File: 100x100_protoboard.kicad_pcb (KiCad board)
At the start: 2 copper layers, 97.8 x 96.5 mm, 422 parts, among them CON1 BARREL_JACK, CON2 USB_FEMALE_WITH_ID, CON3 USB_FEMALE_WITH_ID, J1 INTERCONNECT_1X03, J10 INTERCONNECT_1X03, J11 INTERCONNECT_1X03, J12 INTERCONNECT_1X03, J13 INTERCONNECT_1X03, J14 INTERCONNECT_1X03, J15 INTERCONNECT_1X03, J16 INTERCONNECT_1X03, J17 INTERCONNECT_1X03, J18 INTERCONNECT_1X03, J19 INTERCONNECT_1X03, J2 INTERCONNECT_1X03, J20 INTERCONNECT_1X03, J21 INTERCONNECT_1X03, J22 INTERCONNECT_1X03, J23 INTERCONNECT_1X03, J24 INTERCONNECT_1X03, J25 INTERCONNECT_1X03, J26 INTERCONNECT_1X03, J27 INTERCONNECT_1X03, J28 INTERCONNECT_1X03, J29 INTERCONNECT_1X03, J3 INTERCONNECT_1X03, J30 INTERCONNECT_1X03, J31 INTERCONNECT_1X03, J32 INTERCONNECT_1X03, J33 INTERCONNECT_1X03, J34 INTERCONNECT_1X03, J35 INTERCONNECT_1X03, J36 INTERCONNECT_1X03, J37 INTERCONNECT_1X03, J38 INTERCONNECT_1X03, J39 INTERCONNECT_1X03, J4 INTERCONNECT_1X03, J40 INTERCONNECT_1X03, J41 INTERCONNECT_1X03, J42 INTERCONNECT_1X03, J43 INTERCONNECT_1X03, J44 INTERCONNECT_1X03, J45 INTERCONNECT_1X03, J46 INTERCONNECT_1X03, J47 INTERCONNECT_1X03, J48 INTERCONNECT_1X03, J49 INTERCONNECT_1X03, J5 INTERCONNECT_1X03, J50 INTERCONNECT_1X03, J51 INTERCONNECT_1X03, J52 INTERCONNECT_1X03, J53 INTERCONNECT_1X03, J54 INTERCONNECT_1X03, J55 INTERCONNECT_1X03, J56 INTERCONNECT_1X03, J57 INTERCONNECT_1X03, J58 INTERCONNECT_1X03, J59 INTERCONNECT_1X03, J6 INTERCONNECT_1X03, J60 INTERCONNECT_1X03, J61 INTERCONNECT_1X03, J62 INTERCONNECT_1X03, J63 INTERCONNECT_1X03, J64 INTERCONNECT_1X03, J65 INTERCONNECT_1X02, J7 INTERCONNECT_1X03, J8 INTERCONNECT_1X03, J9 INTERCONNECT_1X03, P1 CONN_5, P1 CONN_6X2, P2 CONN_6X2, U1 LM7805CT

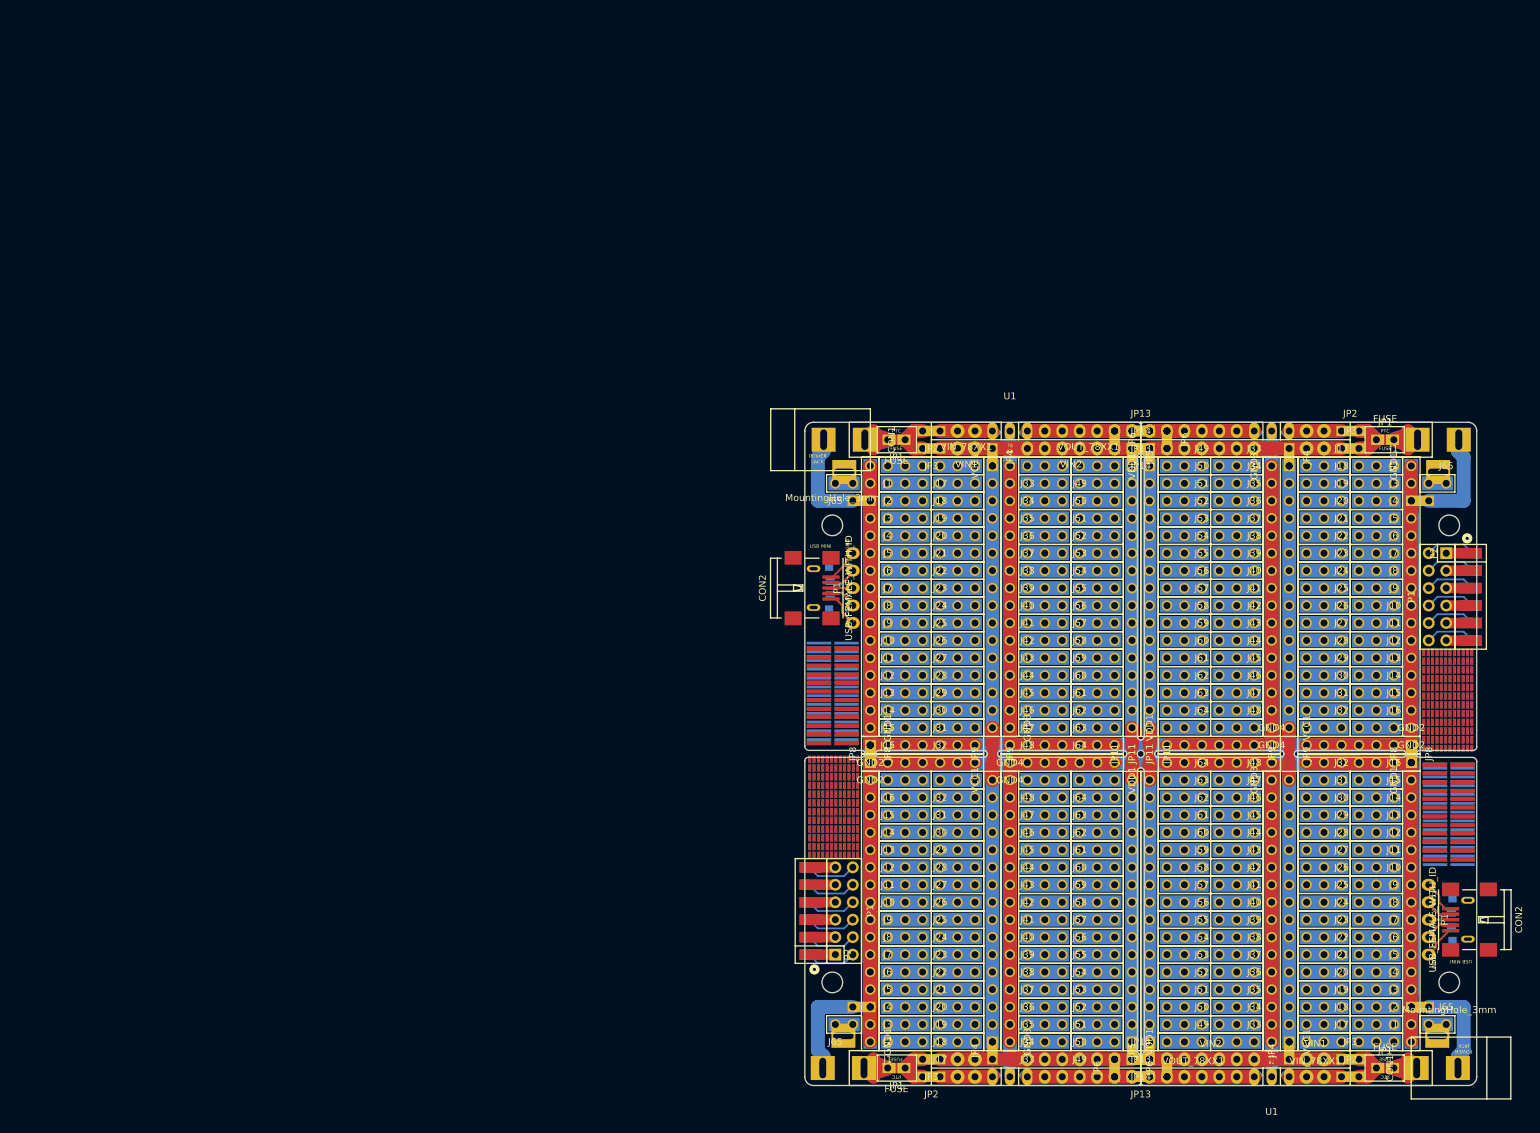
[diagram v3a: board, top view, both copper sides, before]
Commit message: increased .1" edge connector from 2*6 to 2*8 to account for the A-100 system bus used in modular synthesizers
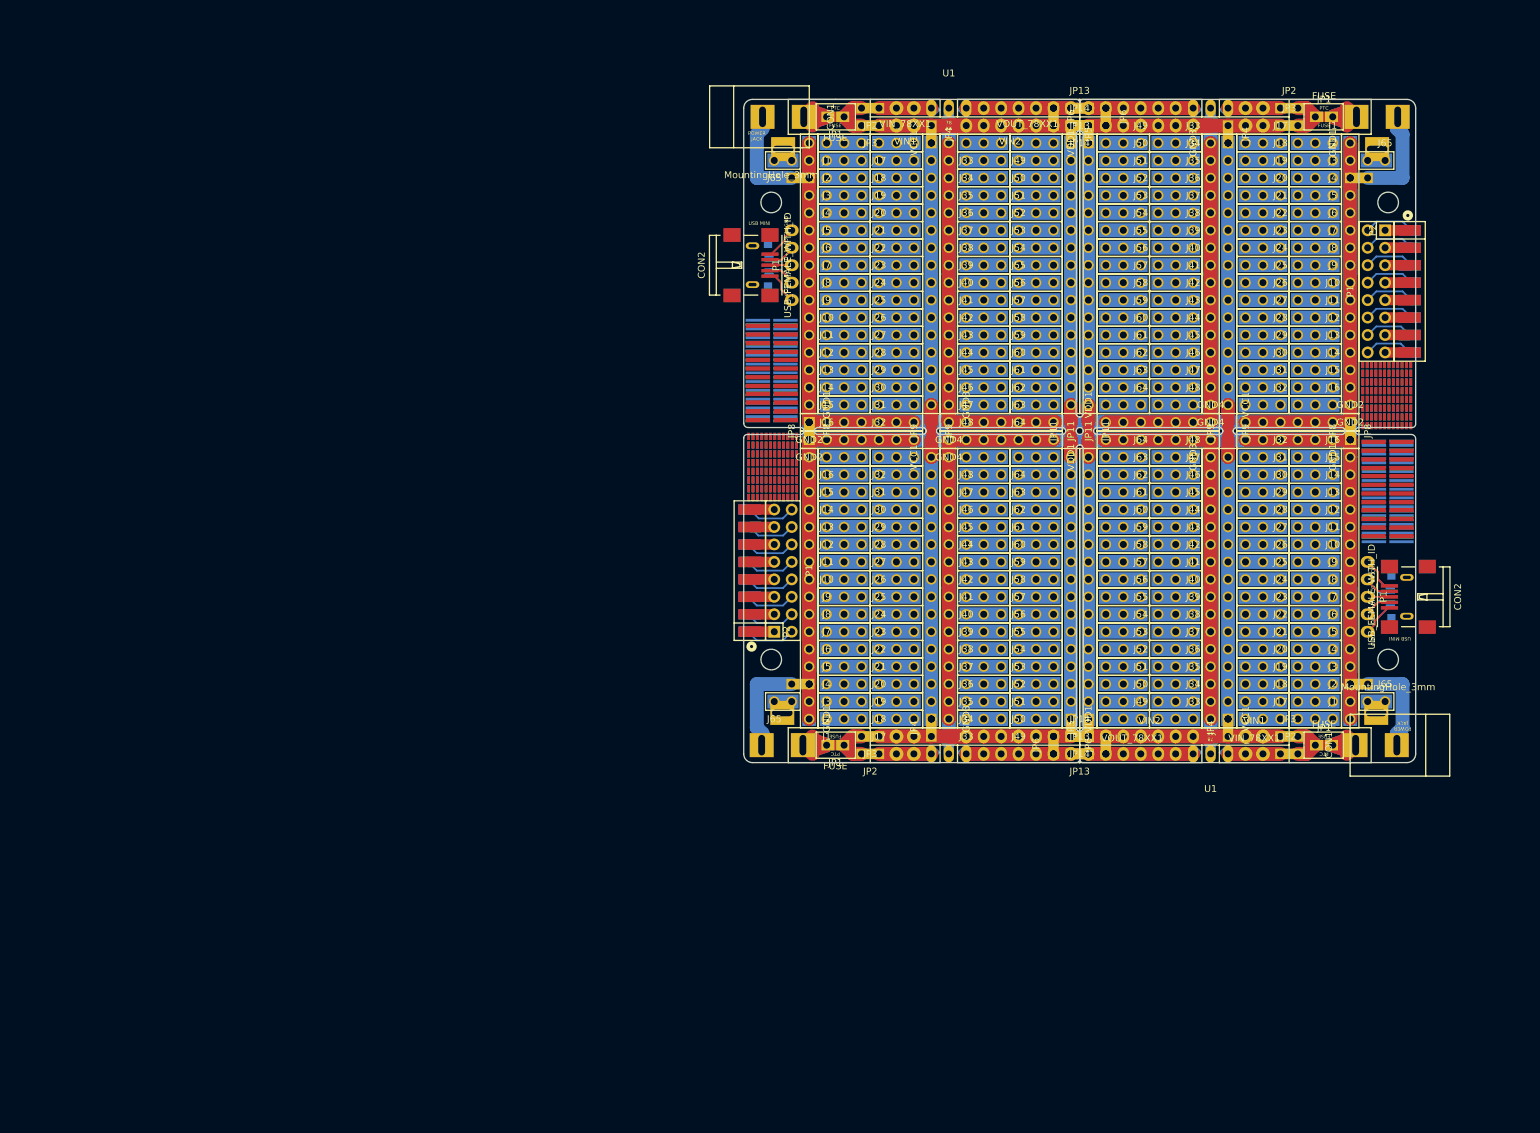
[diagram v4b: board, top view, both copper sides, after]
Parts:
- removed the C1 at (199.4, 79.8)
- removed the C1 at (199.4, 171.7)
- removed the C2 at (196.8, 79.8)
- removed the C2 at (196.8, 171.7)
- removed the CON1 at (225.6, 80.0)
- removed the CON1 at (225.4, 171.4)
- removed the F1 at (214.6, 80.0)
- removed the F1 at (214.6, 171.4)
- removed the F2 at (214.6, 80.0)
- removed the F2 at (214.6, 171.4)
- removed the GND1 at (218.4, 83.8)
- removed the GND1 at (218.4, 129.5)
- removed the GND2 at (218.4, 124.5)
- removed the GND2 at (218.4, 127.0)
- removed the GND3 at (198.1, 83.8)
- removed the GND3 at (198.1, 129.5)
- removed the GND4 at (198.1, 124.5)
- removed the GND4 at (198.1, 127.0)
- removed the J1 at (215.9, 83.8)
- removed the J1 at (215.9, 167.6)
- removed the J10 at (215.9, 106.7)
- removed the J10 at (215.9, 144.8)
- removed the J11 at (215.9, 109.2)
- removed the J11 at (215.9, 142.2)
- removed the J12 at (215.9, 111.8)
- removed the J12 at (215.9, 139.7)
- removed the J13 at (215.9, 114.3)
- removed the J13 at (215.9, 137.2)
- removed the J14 at (215.9, 116.8)
- removed the J14 at (215.9, 134.6)
- removed the J15 at (215.9, 119.4)
- removed the J15 at (215.9, 132.1)
- removed the J16 at (215.9, 121.9)
- removed the J16 at (215.9, 129.5)
- removed the J17 at (208.3, 83.8)
- removed the J17 at (208.3, 167.6)
- removed the J18 at (208.3, 86.4)
- removed the J18 at (208.3, 165.1)
- removed the J19 at (208.3, 88.9)
- removed the J19 at (208.3, 162.6)
- removed the J2 at (215.9, 86.4)
- removed the J2 at (215.9, 165.1)
- removed the J20 at (208.3, 91.4)
- removed the J20 at (208.3, 160.0)
- removed the J21 at (208.3, 94.0)
- removed the J21 at (208.3, 157.5)
- removed the J22 at (208.3, 96.5)
- removed the J22 at (208.3, 154.9)
- removed the J23 at (208.3, 99.1)
- removed the J23 at (208.3, 152.4)
- removed the J24 at (208.3, 101.6)
- removed the J24 at (208.3, 149.9)
- removed the J25 at (208.3, 104.1)
- removed the J25 at (208.3, 147.3)
- removed the J26 at (208.3, 106.7)
- removed the J26 at (208.3, 144.8)
- removed the J27 at (208.3, 109.2)
- removed the J27 at (208.3, 142.2)
- removed the J28 at (208.3, 111.8)
- removed the J28 at (208.3, 139.7)
- removed the J29 at (208.3, 114.3)
- removed the J29 at (208.3, 137.2)
- removed the J3 at (215.9, 88.9)
- removed the J3 at (215.9, 162.6)
- removed the J30 at (208.3, 116.8)
- removed the J30 at (208.3, 134.6)
- removed the J31 at (208.3, 119.4)
- removed the J31 at (208.3, 132.1)
- removed the J32 at (208.3, 121.9)
- removed the J32 at (208.3, 129.5)
- removed the J33 at (195.6, 83.8)
- removed the J33 at (195.6, 167.6)
- removed the J34 at (195.6, 86.4)
- removed the J34 at (195.6, 165.1)
- removed the J35 at (195.6, 88.9)
- removed the J35 at (195.6, 162.6)
- removed the J36 at (195.6, 91.4)
- removed the J36 at (195.6, 160.0)
- removed the J37 at (195.6, 94.0)
- removed the J37 at (195.6, 157.5)
- removed the J38 at (195.6, 96.5)
- removed the J38 at (195.6, 154.9)
- removed the J39 at (195.6, 99.1)
- removed the J39 at (195.6, 152.4)
- removed the J4 at (215.9, 91.4)
- removed the J4 at (215.9, 160.0)
- removed the J40 at (195.6, 101.6)
- removed the J40 at (195.6, 149.9)
- removed the J41 at (195.6, 104.1)
- removed the J41 at (195.6, 147.3)
- removed the J42 at (195.6, 106.7)
- removed the J42 at (195.6, 144.8)
- removed the J43 at (195.6, 109.2)
- removed the J43 at (195.6, 142.2)
- removed the J44 at (195.6, 111.8)
- removed the J44 at (195.6, 139.7)
- removed the J45 at (195.6, 114.3)
- removed the J45 at (195.6, 137.2)
- removed the J46 at (195.6, 116.8)
- removed the J46 at (195.6, 134.6)
- removed the J47 at (195.6, 119.4)
- removed the J47 at (195.6, 132.1)
- removed the J48 at (195.6, 121.9)
- removed the J48 at (195.6, 129.5)
- removed the J49 at (188.0, 83.8)
- removed the J49 at (188.0, 167.6)
- removed the J5 at (215.9, 94.0)
- removed the J5 at (215.9, 157.5)
- removed the J50 at (188.0, 86.4)
- removed the J50 at (188.0, 165.1)
- removed the J51 at (188.0, 88.9)
- removed the J51 at (188.0, 162.6)
- removed the J52 at (188.0, 91.4)
- removed the J52 at (188.0, 160.0)
- removed the J53 at (188.0, 94.0)
- removed the J53 at (188.0, 157.5)
- removed the J54 at (188.0, 96.5)
- removed the J54 at (188.0, 154.9)
- removed the J55 at (188.0, 99.1)
- removed the J55 at (188.0, 152.4)
- removed the J56 at (188.0, 101.6)
- removed the J56 at (188.0, 149.9)
- removed the J57 at (188.0, 104.1)
- removed the J57 at (188.0, 147.3)
- removed the J58 at (188.0, 106.7)
- removed the J58 at (188.0, 144.8)
- removed the J59 at (188.0, 109.2)
- removed the J59 at (188.0, 142.2)
- removed the J6 at (215.9, 96.5)
- removed the J6 at (215.9, 154.9)
- removed the J60 at (188.0, 111.8)
- removed the J60 at (188.0, 139.7)
- removed the J61 at (188.0, 114.3)
- removed the J61 at (188.0, 137.2)
- removed the J62 at (188.0, 116.8)
- removed the J62 at (188.0, 134.6)
- removed the J63 at (188.0, 119.4)
- removed the J63 at (188.0, 132.1)
- removed the J64 at (188.0, 121.9)
- removed the J64 at (188.0, 129.5)
- removed the J65 at (223.5, 86.4)
- removed the J65 at (223.5, 165.1)
- removed the J7 at (215.9, 99.1)
- removed the J7 at (215.9, 152.4)
- removed the J8 at (215.9, 101.6)
- removed the J8 at (215.9, 149.9)
- removed the J9 at (215.9, 104.1)
- removed the J9 at (215.9, 147.3)
- removed the JP1 at (214.6, 80.0)
- removed the JP1 at (214.6, 171.4)
- removed the JP10 at (180.3, 125.7) (x2)
- removed the JP11 at (180.3, 125.7) (x2)
- removed the JP12 at (179.1, 124.5)
- removed the JP12 at (179.1, 127.0)
- removed the JP13 at (179.1, 78.7)
- removed the JP13 at (179.1, 172.7)
- removed the JP14 at (179.1, 81.3)
- removed the JP14 at (179.1, 170.2)
- removed the JP15 at (200.7, 125.7) (x2)
- removed the JP2 at (209.6, 78.7)
- removed the JP2 at (209.6, 172.7)
- removed the JP3 at (209.6, 81.3)
- removed the JP3 at (209.6, 170.2)
- removed the JP4 at (200.7, 82.5)
- removed the JP4 at (200.7, 168.9)
- removed the JP5 at (180.3, 82.5)
- removed the JP5 at (180.3, 168.9)
- removed the JP6 at (182.9, 80.0)
- removed the JP6 at (182.9, 171.4)
- removed the JP7 at (219.7, 88.9)
- removed the JP7 at (219.7, 162.6)
- removed the JP8 at (218.4, 125.7) (x2)
- removed the JP9 at (200.7, 125.7) (x2)
- removed the MountingHole_3mm at (224.0, 92.5)
- removed the MountingHole_3mm at (224.0, 159.0)
- removed the P1 at (222.2, 102.9)
- removed the P1 at (221.0, 149.9)
- removed the P1 at (135.9, 148.6)
- removed the P2 at (227.1, 96.5)
- removed the P2 at (131.1, 154.9)
- removed the Ref** at (224.4, 123.0) (x2)
- removed the Ref** at (223.9, 129.4)
- removed the Ref** at (223.9, 134.5)
- removed the Ref** at (223.9, 139.6)
- removed the Ref** at (133.7, 138.6) (x2)
- removed the Ref** at (224.4, 118.0) (x2)
- removed the Ref** at (224.4, 112.9) (x2)
- removed the Ref** at (223.9, 139.1)
- removed the Ref** at (223.9, 134.2)
- removed the Ref** at (223.9, 129.2)
- removed the U1 at (198.1, 78.7)
- removed the U1 at (198.1, 172.7)
- removed the VCC1 at (200.7, 121.9)
- removed the VCC1 at (200.7, 167.6)
- removed the VDD1 at (180.3, 83.8)
- removed the VDD1 at (180.3, 129.5)
- removed the VIN1 at (204.5, 81.3)
- removed the VIN1 at (204.5, 170.2)
- removed the VIN2 at (189.2, 81.3)
- removed the VIN2 at (189.2, 170.2)
- removed the VIN_78XX1 at (204.5, 78.7)
- removed the VIN_78XX1 at (204.5, 172.7)
- removed the VOUT_78XX1 at (186.7, 78.7)
- removed the VOUT_78XX1 at (186.7, 172.7)
- added C1: u33, Capacitors_SMD:C_0805_HandSoldering, B.Cu at (190.5, 32.8)
- added C1: u33, Capacitors_SMD:C_0805_HandSoldering, B.Cu at (190.5, 124.7)
- added C2: u1, Capacitors_SMD:C_0805_HandSoldering, B.Cu at (188.0, 32.8)
- added C2: u1, Capacitors_SMD:C_0805_HandSoldering, B.Cu at (188.0, 124.7)
- added CON1: BARREL_JACK, Connect:BARREL_JACK, B.Cu at (216.7, 33.0)
- added CON1: BARREL_JACK, Connect:BARREL_JACK, F.Cu at (216.5, 124.5)
- added F1: FUSE, Muonde:CC12ZZ, B.Cu at (205.7, 33.0)
- added F1: FUSE, Muonde:CC12ZZ, F.Cu at (205.7, 124.5)
- added F2: FUSE, Muonde:CC12ZZ, F.Cu at (205.7, 33.0)
- added F2: FUSE, Muonde:CC12ZZ, B.Cu at (205.7, 124.5)
- added GND1: INTERCONNECT_1X16, 2.54mm_Pin_Headers:Interconnect_1x16, F.Cu at (209.6, 36.8)
- added GND1: INTERCONNECT_1X16, 2.54mm_Pin_Headers:Interconnect_1x16, F.Cu at (209.6, 82.5)
- added GND2: INTERCONNECT_1X07, 2.54mm_Pin_Headers:Interconnect_1x07, F.Cu at (209.6, 77.5)
- added GND2: INTERCONNECT_1X07, 2.54mm_Pin_Headers:Interconnect_1x07, F.Cu at (209.6, 80.0)
- added GND3: INTERCONNECT_1X16, 2.54mm_Pin_Headers:Interconnect_1x16, F.Cu at (189.2, 36.8)
- added GND3: INTERCONNECT_1X16, 2.54mm_Pin_Headers:Interconnect_1x16, F.Cu at (189.2, 82.5)
- added GND4: INTERCONNECT_1X07, 2.54mm_Pin_Headers:Interconnect_1x07, F.Cu at (189.2, 77.5)
- added GND4: INTERCONNECT_1X07, 2.54mm_Pin_Headers:Interconnect_1x07, F.Cu at (189.2, 80.0)
- added J1: INTERCONNECT_1X03, 2.54mm_Pin_Headers:Interconnect_1x03, F.Cu at (207.0, 36.8)
- added J1: INTERCONNECT_1X03, 2.54mm_Pin_Headers:Interconnect_1x03, F.Cu at (207.0, 120.7)
- added J10: INTERCONNECT_1X03, 2.54mm_Pin_Headers:Interconnect_1x03, F.Cu at (207.0, 59.7)
- added J10: INTERCONNECT_1X03, 2.54mm_Pin_Headers:Interconnect_1x03, F.Cu at (207.0, 97.8)
- added J11: INTERCONNECT_1X03, 2.54mm_Pin_Headers:Interconnect_1x03, F.Cu at (207.0, 62.2)
- added J11: INTERCONNECT_1X03, 2.54mm_Pin_Headers:Interconnect_1x03, F.Cu at (207.0, 95.2)
- added J12: INTERCONNECT_1X03, 2.54mm_Pin_Headers:Interconnect_1x03, F.Cu at (207.0, 64.8)
- added J12: INTERCONNECT_1X03, 2.54mm_Pin_Headers:Interconnect_1x03, F.Cu at (207.0, 92.7)
- added J13: INTERCONNECT_1X03, 2.54mm_Pin_Headers:Interconnect_1x03, F.Cu at (207.0, 67.3)
- added J13: INTERCONNECT_1X03, 2.54mm_Pin_Headers:Interconnect_1x03, F.Cu at (207.0, 90.2)
- added J14: INTERCONNECT_1X03, 2.54mm_Pin_Headers:Interconnect_1x03, F.Cu at (207.0, 69.8)
- added J14: INTERCONNECT_1X03, 2.54mm_Pin_Headers:Interconnect_1x03, F.Cu at (207.0, 87.6)
- added J15: INTERCONNECT_1X03, 2.54mm_Pin_Headers:Interconnect_1x03, F.Cu at (207.0, 72.4)
- added J15: INTERCONNECT_1X03, 2.54mm_Pin_Headers:Interconnect_1x03, F.Cu at (207.0, 85.1)
- added J16: INTERCONNECT_1X03, 2.54mm_Pin_Headers:Interconnect_1x03, F.Cu at (207.0, 74.9)
- added J16: INTERCONNECT_1X03, 2.54mm_Pin_Headers:Interconnect_1x03, F.Cu at (207.0, 82.5)
- added J17: INTERCONNECT_1X03, 2.54mm_Pin_Headers:Interconnect_1x03, F.Cu at (199.4, 36.8)
- added J17: INTERCONNECT_1X03, 2.54mm_Pin_Headers:Interconnect_1x03, F.Cu at (199.4, 120.7)
- added J18: INTERCONNECT_1X03, 2.54mm_Pin_Headers:Interconnect_1x03, F.Cu at (199.4, 39.4)
- added J18: INTERCONNECT_1X03, 2.54mm_Pin_Headers:Interconnect_1x03, F.Cu at (199.4, 118.1)
- added J19: INTERCONNECT_1X03, 2.54mm_Pin_Headers:Interconnect_1x03, F.Cu at (199.4, 41.9)
- added J19: INTERCONNECT_1X03, 2.54mm_Pin_Headers:Interconnect_1x03, F.Cu at (199.4, 115.6)
- added J2: INTERCONNECT_1X03, 2.54mm_Pin_Headers:Interconnect_1x03, F.Cu at (207.0, 39.4)
- added J2: INTERCONNECT_1X03, 2.54mm_Pin_Headers:Interconnect_1x03, F.Cu at (207.0, 118.1)
- added J20: INTERCONNECT_1X03, 2.54mm_Pin_Headers:Interconnect_1x03, F.Cu at (199.4, 44.5)
- added J20: INTERCONNECT_1X03, 2.54mm_Pin_Headers:Interconnect_1x03, F.Cu at (199.4, 113.0)
- added J21: INTERCONNECT_1X03, 2.54mm_Pin_Headers:Interconnect_1x03, F.Cu at (199.4, 47.0)
- added J21: INTERCONNECT_1X03, 2.54mm_Pin_Headers:Interconnect_1x03, F.Cu at (199.4, 110.5)
- added J22: INTERCONNECT_1X03, 2.54mm_Pin_Headers:Interconnect_1x03, F.Cu at (199.4, 49.5)
- added J22: INTERCONNECT_1X03, 2.54mm_Pin_Headers:Interconnect_1x03, F.Cu at (199.4, 108.0)
- added J23: INTERCONNECT_1X03, 2.54mm_Pin_Headers:Interconnect_1x03, F.Cu at (199.4, 52.1)
- added J23: INTERCONNECT_1X03, 2.54mm_Pin_Headers:Interconnect_1x03, F.Cu at (199.4, 105.4)
- added J24: INTERCONNECT_1X03, 2.54mm_Pin_Headers:Interconnect_1x03, F.Cu at (199.4, 54.6)
- added J24: INTERCONNECT_1X03, 2.54mm_Pin_Headers:Interconnect_1x03, F.Cu at (199.4, 102.9)
- added J25: INTERCONNECT_1X03, 2.54mm_Pin_Headers:Interconnect_1x03, F.Cu at (199.4, 57.1)
- added J25: INTERCONNECT_1X03, 2.54mm_Pin_Headers:Interconnect_1x03, F.Cu at (199.4, 100.3)
- added J26: INTERCONNECT_1X03, 2.54mm_Pin_Headers:Interconnect_1x03, F.Cu at (199.4, 59.7)
- added J26: INTERCONNECT_1X03, 2.54mm_Pin_Headers:Interconnect_1x03, F.Cu at (199.4, 97.8)
- added J27: INTERCONNECT_1X03, 2.54mm_Pin_Headers:Interconnect_1x03, F.Cu at (199.4, 62.2)
- added J27: INTERCONNECT_1X03, 2.54mm_Pin_Headers:Interconnect_1x03, F.Cu at (199.4, 95.2)
- added J28: INTERCONNECT_1X03, 2.54mm_Pin_Headers:Interconnect_1x03, F.Cu at (199.4, 64.8)
- added J28: INTERCONNECT_1X03, 2.54mm_Pin_Headers:Interconnect_1x03, F.Cu at (199.4, 92.7)
- added J29: INTERCONNECT_1X03, 2.54mm_Pin_Headers:Interconnect_1x03, F.Cu at (199.4, 67.3)
- added J29: INTERCONNECT_1X03, 2.54mm_Pin_Headers:Interconnect_1x03, F.Cu at (199.4, 90.2)
- added J3: INTERCONNECT_1X03, 2.54mm_Pin_Headers:Interconnect_1x03, F.Cu at (207.0, 41.9)
- added J3: INTERCONNECT_1X03, 2.54mm_Pin_Headers:Interconnect_1x03, F.Cu at (207.0, 115.6)
- added J30: INTERCONNECT_1X03, 2.54mm_Pin_Headers:Interconnect_1x03, F.Cu at (199.4, 69.8)
- added J30: INTERCONNECT_1X03, 2.54mm_Pin_Headers:Interconnect_1x03, F.Cu at (199.4, 87.6)
- added J31: INTERCONNECT_1X03, 2.54mm_Pin_Headers:Interconnect_1x03, F.Cu at (199.4, 72.4)
- added J31: INTERCONNECT_1X03, 2.54mm_Pin_Headers:Interconnect_1x03, F.Cu at (199.4, 85.1)
- added J32: INTERCONNECT_1X03, 2.54mm_Pin_Headers:Interconnect_1x03, F.Cu at (199.4, 74.9)
- added J32: INTERCONNECT_1X03, 2.54mm_Pin_Headers:Interconnect_1x03, F.Cu at (199.4, 82.5)
- added J33: INTERCONNECT_1X03, 2.54mm_Pin_Headers:Interconnect_1x03, F.Cu at (186.7, 36.8)
- added J33: INTERCONNECT_1X03, 2.54mm_Pin_Headers:Interconnect_1x03, F.Cu at (186.7, 120.7)
- added J34: INTERCONNECT_1X03, 2.54mm_Pin_Headers:Interconnect_1x03, F.Cu at (186.7, 39.4)
- added J34: INTERCONNECT_1X03, 2.54mm_Pin_Headers:Interconnect_1x03, F.Cu at (186.7, 118.1)
- added J35: INTERCONNECT_1X03, 2.54mm_Pin_Headers:Interconnect_1x03, F.Cu at (186.7, 41.9)
- added J35: INTERCONNECT_1X03, 2.54mm_Pin_Headers:Interconnect_1x03, F.Cu at (186.7, 115.6)
- added J36: INTERCONNECT_1X03, 2.54mm_Pin_Headers:Interconnect_1x03, F.Cu at (186.7, 44.5)
- added J36: INTERCONNECT_1X03, 2.54mm_Pin_Headers:Interconnect_1x03, F.Cu at (186.7, 113.0)
- added J37: INTERCONNECT_1X03, 2.54mm_Pin_Headers:Interconnect_1x03, F.Cu at (186.7, 47.0)
- added J37: INTERCONNECT_1X03, 2.54mm_Pin_Headers:Interconnect_1x03, F.Cu at (186.7, 110.5)
- added J38: INTERCONNECT_1X03, 2.54mm_Pin_Headers:Interconnect_1x03, F.Cu at (186.7, 49.5)
- added J38: INTERCONNECT_1X03, 2.54mm_Pin_Headers:Interconnect_1x03, F.Cu at (186.7, 108.0)
- added J39: INTERCONNECT_1X03, 2.54mm_Pin_Headers:Interconnect_1x03, F.Cu at (186.7, 52.1)
- added J39: INTERCONNECT_1X03, 2.54mm_Pin_Headers:Interconnect_1x03, F.Cu at (186.7, 105.4)
- added J4: INTERCONNECT_1X03, 2.54mm_Pin_Headers:Interconnect_1x03, F.Cu at (207.0, 44.5)
- added J4: INTERCONNECT_1X03, 2.54mm_Pin_Headers:Interconnect_1x03, F.Cu at (207.0, 113.0)
- added J40: INTERCONNECT_1X03, 2.54mm_Pin_Headers:Interconnect_1x03, F.Cu at (186.7, 54.6)
- added J40: INTERCONNECT_1X03, 2.54mm_Pin_Headers:Interconnect_1x03, F.Cu at (186.7, 102.9)
- added J41: INTERCONNECT_1X03, 2.54mm_Pin_Headers:Interconnect_1x03, F.Cu at (186.7, 57.1)
- added J41: INTERCONNECT_1X03, 2.54mm_Pin_Headers:Interconnect_1x03, F.Cu at (186.7, 100.3)
- added J42: INTERCONNECT_1X03, 2.54mm_Pin_Headers:Interconnect_1x03, F.Cu at (186.7, 59.7)
- added J42: INTERCONNECT_1X03, 2.54mm_Pin_Headers:Interconnect_1x03, F.Cu at (186.7, 97.8)
- added J43: INTERCONNECT_1X03, 2.54mm_Pin_Headers:Interconnect_1x03, F.Cu at (186.7, 62.2)
- added J43: INTERCONNECT_1X03, 2.54mm_Pin_Headers:Interconnect_1x03, F.Cu at (186.7, 95.2)
- added J44: INTERCONNECT_1X03, 2.54mm_Pin_Headers:Interconnect_1x03, F.Cu at (186.7, 64.8)
- added J44: INTERCONNECT_1X03, 2.54mm_Pin_Headers:Interconnect_1x03, F.Cu at (186.7, 92.7)
- added J45: INTERCONNECT_1X03, 2.54mm_Pin_Headers:Interconnect_1x03, F.Cu at (186.7, 67.3)
- added J45: INTERCONNECT_1X03, 2.54mm_Pin_Headers:Interconnect_1x03, F.Cu at (186.7, 90.2)
- added J46: INTERCONNECT_1X03, 2.54mm_Pin_Headers:Interconnect_1x03, F.Cu at (186.7, 69.8)
- added J46: INTERCONNECT_1X03, 2.54mm_Pin_Headers:Interconnect_1x03, F.Cu at (186.7, 87.6)
- added J47: INTERCONNECT_1X03, 2.54mm_Pin_Headers:Interconnect_1x03, F.Cu at (186.7, 72.4)
- added J47: INTERCONNECT_1X03, 2.54mm_Pin_Headers:Interconnect_1x03, F.Cu at (186.7, 85.1)
- added J48: INTERCONNECT_1X03, 2.54mm_Pin_Headers:Interconnect_1x03, F.Cu at (186.7, 74.9)
- added J48: INTERCONNECT_1X03, 2.54mm_Pin_Headers:Interconnect_1x03, F.Cu at (186.7, 82.5)
- added J49: INTERCONNECT_1X03, 2.54mm_Pin_Headers:Interconnect_1x03, F.Cu at (179.1, 36.8)
- added J49: INTERCONNECT_1X03, 2.54mm_Pin_Headers:Interconnect_1x03, F.Cu at (179.1, 120.7)
- added J5: INTERCONNECT_1X03, 2.54mm_Pin_Headers:Interconnect_1x03, F.Cu at (207.0, 47.0)
- added J5: INTERCONNECT_1X03, 2.54mm_Pin_Headers:Interconnect_1x03, F.Cu at (207.0, 110.5)
- added J50: INTERCONNECT_1X03, 2.54mm_Pin_Headers:Interconnect_1x03, F.Cu at (179.1, 39.4)
- added J50: INTERCONNECT_1X03, 2.54mm_Pin_Headers:Interconnect_1x03, F.Cu at (179.1, 118.1)
- added J51: INTERCONNECT_1X03, 2.54mm_Pin_Headers:Interconnect_1x03, F.Cu at (179.1, 41.9)
- added J51: INTERCONNECT_1X03, 2.54mm_Pin_Headers:Interconnect_1x03, F.Cu at (179.1, 115.6)
- added J52: INTERCONNECT_1X03, 2.54mm_Pin_Headers:Interconnect_1x03, F.Cu at (179.1, 44.5)
- added J52: INTERCONNECT_1X03, 2.54mm_Pin_Headers:Interconnect_1x03, F.Cu at (179.1, 113.0)
- added J53: INTERCONNECT_1X03, 2.54mm_Pin_Headers:Interconnect_1x03, F.Cu at (179.1, 47.0)
- added J53: INTERCONNECT_1X03, 2.54mm_Pin_Headers:Interconnect_1x03, F.Cu at (179.1, 110.5)
- added J54: INTERCONNECT_1X03, 2.54mm_Pin_Headers:Interconnect_1x03, F.Cu at (179.1, 49.5)
- added J54: INTERCONNECT_1X03, 2.54mm_Pin_Headers:Interconnect_1x03, F.Cu at (179.1, 108.0)
- added J55: INTERCONNECT_1X03, 2.54mm_Pin_Headers:Interconnect_1x03, F.Cu at (179.1, 52.1)
- added J55: INTERCONNECT_1X03, 2.54mm_Pin_Headers:Interconnect_1x03, F.Cu at (179.1, 105.4)
- added J56: INTERCONNECT_1X03, 2.54mm_Pin_Headers:Interconnect_1x03, F.Cu at (179.1, 54.6)
- added J56: INTERCONNECT_1X03, 2.54mm_Pin_Headers:Interconnect_1x03, F.Cu at (179.1, 102.9)
- added J57: INTERCONNECT_1X03, 2.54mm_Pin_Headers:Interconnect_1x03, F.Cu at (179.1, 57.1)
- added J57: INTERCONNECT_1X03, 2.54mm_Pin_Headers:Interconnect_1x03, F.Cu at (179.1, 100.3)
- added J58: INTERCONNECT_1X03, 2.54mm_Pin_Headers:Interconnect_1x03, F.Cu at (179.1, 59.7)
- added J58: INTERCONNECT_1X03, 2.54mm_Pin_Headers:Interconnect_1x03, F.Cu at (179.1, 97.8)
- added J59: INTERCONNECT_1X03, 2.54mm_Pin_Headers:Interconnect_1x03, F.Cu at (179.1, 62.2)
- added J59: INTERCONNECT_1X03, 2.54mm_Pin_Headers:Interconnect_1x03, F.Cu at (179.1, 95.2)
- added J6: INTERCONNECT_1X03, 2.54mm_Pin_Headers:Interconnect_1x03, F.Cu at (207.0, 49.5)
- added J6: INTERCONNECT_1X03, 2.54mm_Pin_Headers:Interconnect_1x03, F.Cu at (207.0, 108.0)
- added J60: INTERCONNECT_1X03, 2.54mm_Pin_Headers:Interconnect_1x03, F.Cu at (179.1, 64.8)
- added J60: INTERCONNECT_1X03, 2.54mm_Pin_Headers:Interconnect_1x03, F.Cu at (179.1, 92.7)
- added J61: INTERCONNECT_1X03, 2.54mm_Pin_Headers:Interconnect_1x03, F.Cu at (179.1, 67.3)
- added J61: INTERCONNECT_1X03, 2.54mm_Pin_Headers:Interconnect_1x03, F.Cu at (179.1, 90.2)
- added J62: INTERCONNECT_1X03, 2.54mm_Pin_Headers:Interconnect_1x03, F.Cu at (179.1, 69.8)
- added J62: INTERCONNECT_1X03, 2.54mm_Pin_Headers:Interconnect_1x03, F.Cu at (179.1, 87.6)
- added J63: INTERCONNECT_1X03, 2.54mm_Pin_Headers:Interconnect_1x03, F.Cu at (179.1, 72.4)
- added J63: INTERCONNECT_1X03, 2.54mm_Pin_Headers:Interconnect_1x03, F.Cu at (179.1, 85.1)
- added J64: INTERCONNECT_1X03, 2.54mm_Pin_Headers:Interconnect_1x03, F.Cu at (179.1, 74.9)
- added J64: INTERCONNECT_1X03, 2.54mm_Pin_Headers:Interconnect_1x03, F.Cu at (179.1, 82.5)
- added J65: INTERCONNECT_1X02, 2.54mm_Pin_Headers:Interconnect_1x02, F.Cu at (214.6, 39.4)
- added J65: INTERCONNECT_1X02, 2.54mm_Pin_Headers:Interconnect_1x02, F.Cu at (214.6, 118.1)
- added J7: INTERCONNECT_1X03, 2.54mm_Pin_Headers:Interconnect_1x03, F.Cu at (207.0, 52.1)
- added J7: INTERCONNECT_1X03, 2.54mm_Pin_Headers:Interconnect_1x03, F.Cu at (207.0, 105.4)
- added J8: INTERCONNECT_1X03, 2.54mm_Pin_Headers:Interconnect_1x03, F.Cu at (207.0, 54.6)
- added J8: INTERCONNECT_1X03, 2.54mm_Pin_Headers:Interconnect_1x03, F.Cu at (207.0, 102.9)
- added J9: INTERCONNECT_1X03, 2.54mm_Pin_Headers:Interconnect_1x03, F.Cu at (207.0, 57.1)
- added J9: INTERCONNECT_1X03, 2.54mm_Pin_Headers:Interconnect_1x03, F.Cu at (207.0, 100.3)
- added JP1: JUMPER, 2.54mm_Pin_Headers:Solder_Jumper_1x2_Shorted_T, F.Cu at (205.7, 33.0)
- added JP1: JUMPER, 2.54mm_Pin_Headers:Solder_Jumper_1x2_Shorted_T, F.Cu at (205.7, 124.5)
- added JP10 (x2): JUMPER, 2.54mm_Pin_Headers:Solder_Jumper_SMD_1x2_Shorted, B.Cu at (171.4, 78.7)
- added JP11 (x2): JUMPER, 2.54mm_Pin_Headers:Solder_Jumper_SMD_1x2_Shorted, F.Cu at (171.4, 78.7)
- added JP12: JUMPER, 2.54mm_Pin_Headers:Solder_Jumper_SMD_1x2_Shorted, B.Cu at (170.2, 77.5)
- added JP12: JUMPER, 2.54mm_Pin_Headers:Solder_Jumper_SMD_1x2_Shorted, B.Cu at (170.2, 80.0)
- added JP13: JUMPER, 2.54mm_Pin_Headers:Solder_Jumper_1x2_Shorted_T, F.Cu at (170.2, 31.8)
- added JP13: JUMPER, 2.54mm_Pin_Headers:Solder_Jumper_1x2_Shorted_T, F.Cu at (170.2, 125.7)
- added JP14: JUMPER, 2.54mm_Pin_Headers:Solder_Jumper_1x2_Shorted_T, F.Cu at (170.2, 34.3)
- added JP14: JUMPER, 2.54mm_Pin_Headers:Solder_Jumper_1x2_Shorted_T, F.Cu at (170.2, 123.2)
- added JP15 (x2): JUMPER, 2.54mm_Pin_Headers:Solder_Jumper_SMD_1x2, B.Cu at (191.8, 78.7)
- added JP2: JUMPER, 2.54mm_Pin_Headers:Solder_Jumper_1x2_Shorted_T, F.Cu at (200.7, 31.8)
- added JP2: JUMPER, 2.54mm_Pin_Headers:Solder_Jumper_1x2_Shorted_T, F.Cu at (200.7, 125.7)
- added JP3: JUMPER, 2.54mm_Pin_Headers:Solder_Jumper_1x2_Shorted_T, F.Cu at (200.7, 34.3)
- added JP3: JUMPER, 2.54mm_Pin_Headers:Solder_Jumper_1x2_Shorted_T, F.Cu at (200.7, 123.2)
- added JP4: JUMPER, 2.54mm_Pin_Headers:Solder_Jumper_1x2_Shorted_T, F.Cu at (191.8, 35.6)
- added JP4: JUMPER, 2.54mm_Pin_Headers:Solder_Jumper_1x2_Shorted_T, F.Cu at (191.8, 121.9)
- added JP5: JUMPER, 2.54mm_Pin_Headers:Solder_Jumper_1x2_Shorted_T, B.Cu at (171.4, 35.6)
- added JP5: JUMPER, 2.54mm_Pin_Headers:Solder_Jumper_1x2_Shorted_T, F.Cu at (171.4, 121.9)
- added JP6: JUMPER, 2.54mm_Pin_Headers:Solder_Jumper_1x2_Shorted_T, F.Cu at (174.0, 33.0)
- added JP6: JUMPER, 2.54mm_Pin_Headers:Solder_Jumper_1x2_Shorted_T, F.Cu at (174.0, 124.5)
- added JP7: JUMPER, 2.54mm_Pin_Headers:Solder_Jumper_1x2_Shorted_T, B.Cu at (210.8, 41.9)
- added JP7: JUMPER, 2.54mm_Pin_Headers:Solder_Jumper_1x2_Shorted_T, B.Cu at (210.8, 115.6)
- added JP8 (x2): JUMPER, 2.54mm_Pin_Headers:Solder_Jumper_1x2, F.Cu at (209.6, 78.7)
- added JP9 (x2): JUMPER, 2.54mm_Pin_Headers:Solder_Jumper_SMD_1x2_Shorted, F.Cu at (191.8, 78.7)
- added MountingHole_3mm: VAL**, Mounting_Holes:MountingHole_3mm, B.Cu at (215.1, 45.5)
- added MountingHole_3mm: VAL**, Mounting_Holes:MountingHole_3mm, F.Cu at (215.1, 112.0)
- added P1: CONN_8X2, Socket_Strips:Socket_Strip_Straight_2x08, F.Cu at (213.4, 58.4)
- added P1: CONN_5, Socket_Strips:Socket_Strip_Straight_1x05, F.Cu at (212.1, 102.9)
- added P1: CONN_8X2, Socket_Strips:Socket_Strip_Straight_2x08, F.Cu at (127.0, 99.1)
- added P2: CONN_8X2, 2.54mm_Pin_Headers:Edge_2x08, F.Cu at (218.2, 49.5)
- added P2: CONN_8X2, 2.54mm_Pin_Headers:Edge_2x08, F.Cu at (122.2, 108.0)
- added Ref**: Val**, SMD:SMD_127_065_grid_4X12, F.Cu at (215.5, 76.0)
- added Ref**: Val**, SMD:SMD_065_357_8X2, B.Cu at (215.0, 92.6)
- added Ref**: Val**, SMD:SMD_127_065_grid_4X12, F.Cu at (215.5, 71.0)
- added Ref**: Val**, SMD:SMD_127_065_grid_4X12, B.Cu at (215.5, 76.0)
- added Ref**: Val**, SMD:SMD_127_065_grid_4X12, B.Cu at (215.5, 71.0)
- added Ref**: Val**, SMD:SMD_127_357_4X2, F.Cu at (215.0, 92.2)
- added Ref**: Val**, SMD:SMD_127_357_4X2, F.Cu at (215.0, 87.2)
- added Ref**: Val**, SMD:SMD_127_357_4X2, F.Cu at (215.0, 82.2)
- added Ref**: Val**, SMD:SMD_065_357_8X2, B.Cu at (215.0, 82.4)
- added Ref**: Val**, SMD:SMD_065_357_8X2, B.Cu at (215.0, 87.5)
- added U1: LM7805CT, Transistors_TO-220:TO-220_Neutral123_Vertical, B.Cu at (189.2, 31.8)
- added U1: LM7805CT, Transistors_TO-220:TO-220_Neutral123_Vertical, F.Cu at (189.2, 125.7)
- added VCC1: INTERCONNECT_1X16, 2.54mm_Pin_Headers:Interconnect_1x16, F.Cu at (191.8, 74.9)
- added VCC1: INTERCONNECT_1X16, 2.54mm_Pin_Headers:Interconnect_1x16, F.Cu at (191.8, 120.7)
- added VDD1: INTERCONNECT_1X16, 2.54mm_Pin_Headers:Interconnect_1x16, F.Cu at (171.4, 36.8)
- added VDD1: INTERCONNECT_1X16, 2.54mm_Pin_Headers:Interconnect_1x16, F.Cu at (171.4, 82.5)
- added VIN1: CONN_2, Socket_Strips:Socket_Strip_Straight_1x02, B.Cu at (195.6, 34.3)
- added VIN1: CONN_2, Socket_Strips:Socket_Strip_Straight_1x02, F.Cu at (195.6, 123.2)
- added VIN2: CONN_6, Socket_Strips:Socket_Strip_Straight_1x06, B.Cu at (180.3, 34.3)
- added VIN2: CONN_6, Socket_Strips:Socket_Strip_Straight_1x06, F.Cu at (180.3, 123.2)
- added VIN_78XX1: CONN_2, Socket_Strips:Socket_Strip_Straight_1x02, B.Cu at (195.6, 31.8)
- added VIN_78XX1: CONN_2, Socket_Strips:Socket_Strip_Straight_1x02, F.Cu at (195.6, 125.7)
- added VOUT_78XX1: CONN_6, Socket_Strips:Socket_Strip_Straight_1x06, B.Cu at (177.8, 31.8)
- added VOUT_78XX1: CONN_6, Socket_Strips:Socket_Strip_Straight_1x06, F.Cu at (177.8, 125.7)
- moved C1 47.8 mm to (149.9, 124.7)
- moved C2 47.8 mm to (152.4, 124.7)
- moved CON2 47.8 mm to (215.3, 102.9)
- moved CON3 47.8 mm to (215.4, 102.9)
- moved J10 47.8 mm to (133.3, 59.7)
- moved J11 47.8 mm to (133.3, 95.2)
- moved J12 47.8 mm to (133.3, 64.8)
- moved J14 47.8 mm to (133.3, 69.8)
- moved J14 47.8 mm to (133.3, 87.6)
- moved J15 47.8 mm to (133.3, 85.1)
- moved J19 47.8 mm to (141.0, 41.9)
- moved J19 47.8 mm to (141.0, 115.6)
- moved J20 47.8 mm to (141.0, 113.0)
- moved J23 47.8 mm to (141.0, 105.4)
- moved J24 47.8 mm to (141.0, 102.9)
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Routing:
- net Net-(JP8-Pad2): track 74.9 -> 40.6 mm
- net Net-(JP15-Pad2): track 0.00 -> 20.3 mm
- net Net-(P1-Pad16): track 0.00 -> 16.1 mm
- net Net-(P1-Pad14): track 0.00 -> 16.0 mm
- net Net-(C1-Pad2): track 989.4 -> 1003.4 mm
- net Net-(P1-Pad15): track 0.00 -> 7.11 mm
- net Net-(P1-Pad13): track 0.00 -> 7.11 mm
- net Net-(JP11-Pad2): track 5.08 -> 2.54 mm
- net Net-(JP11-Pad1): track 5.08 -> 7.62 mm
